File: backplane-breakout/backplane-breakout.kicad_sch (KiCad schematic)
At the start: 12 parts, among them J101 Backplane

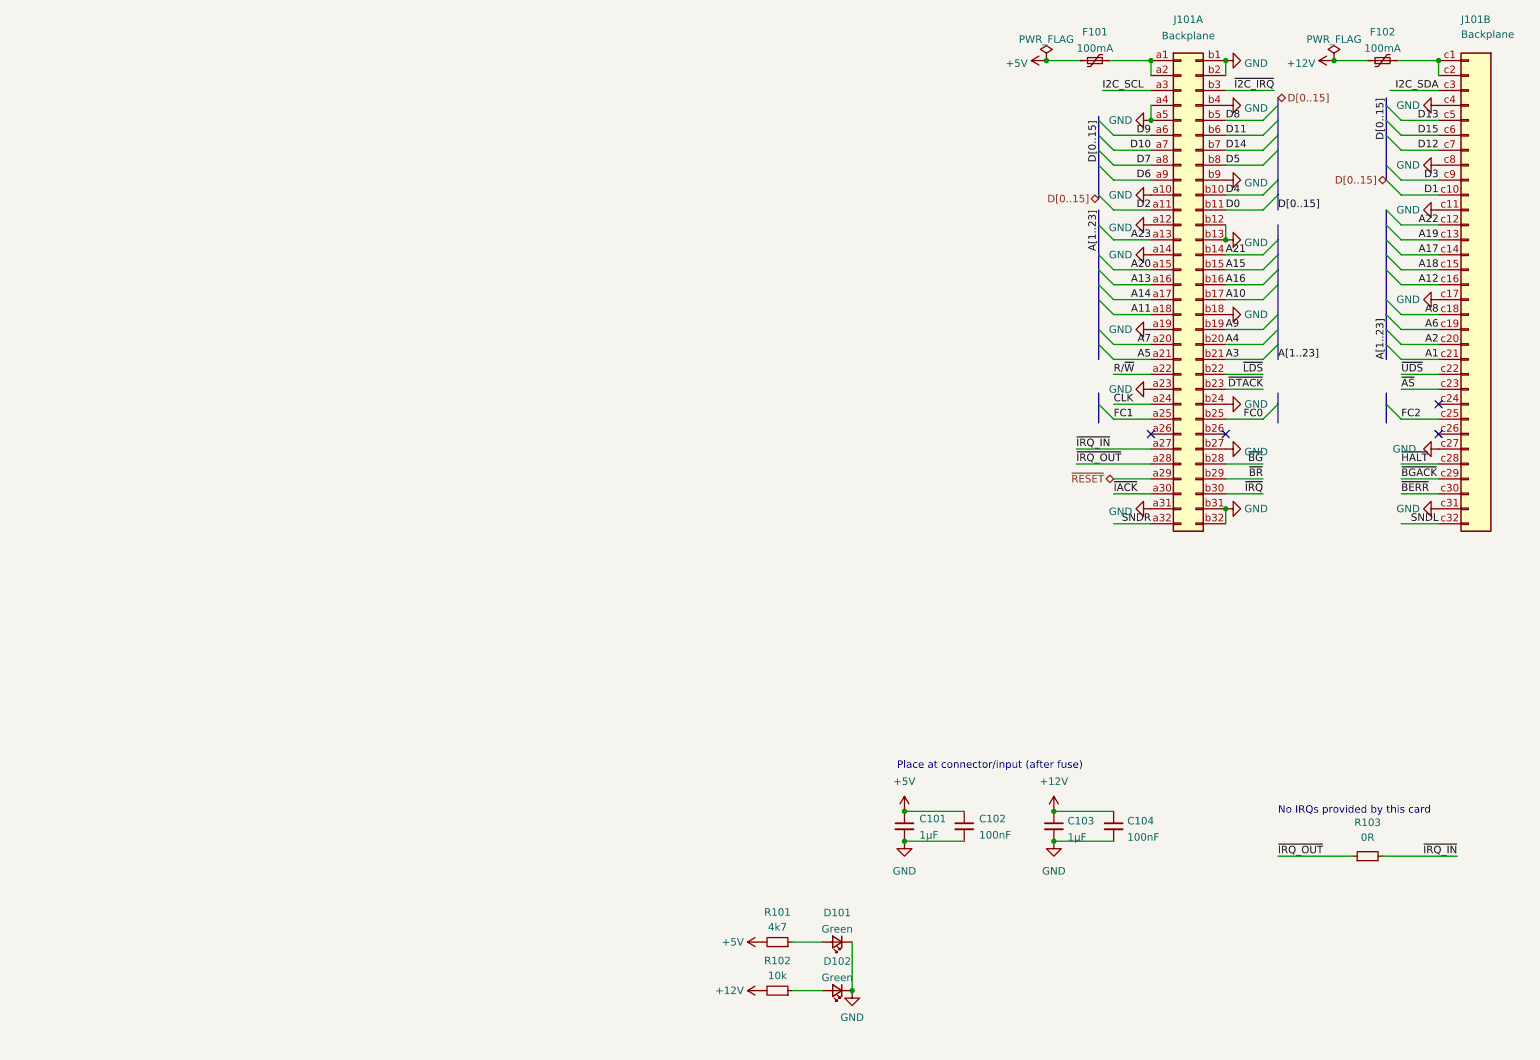
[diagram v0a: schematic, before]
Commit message: Finished backplane breakout
- All of the backplane signals (for an expansion card) are brought out
  to 2x10 headers, which can connect to the logic analyzer through
  isolation adapters or direct probing in a more compact pinout

- Added a footprint for a shrouded 2x10 header
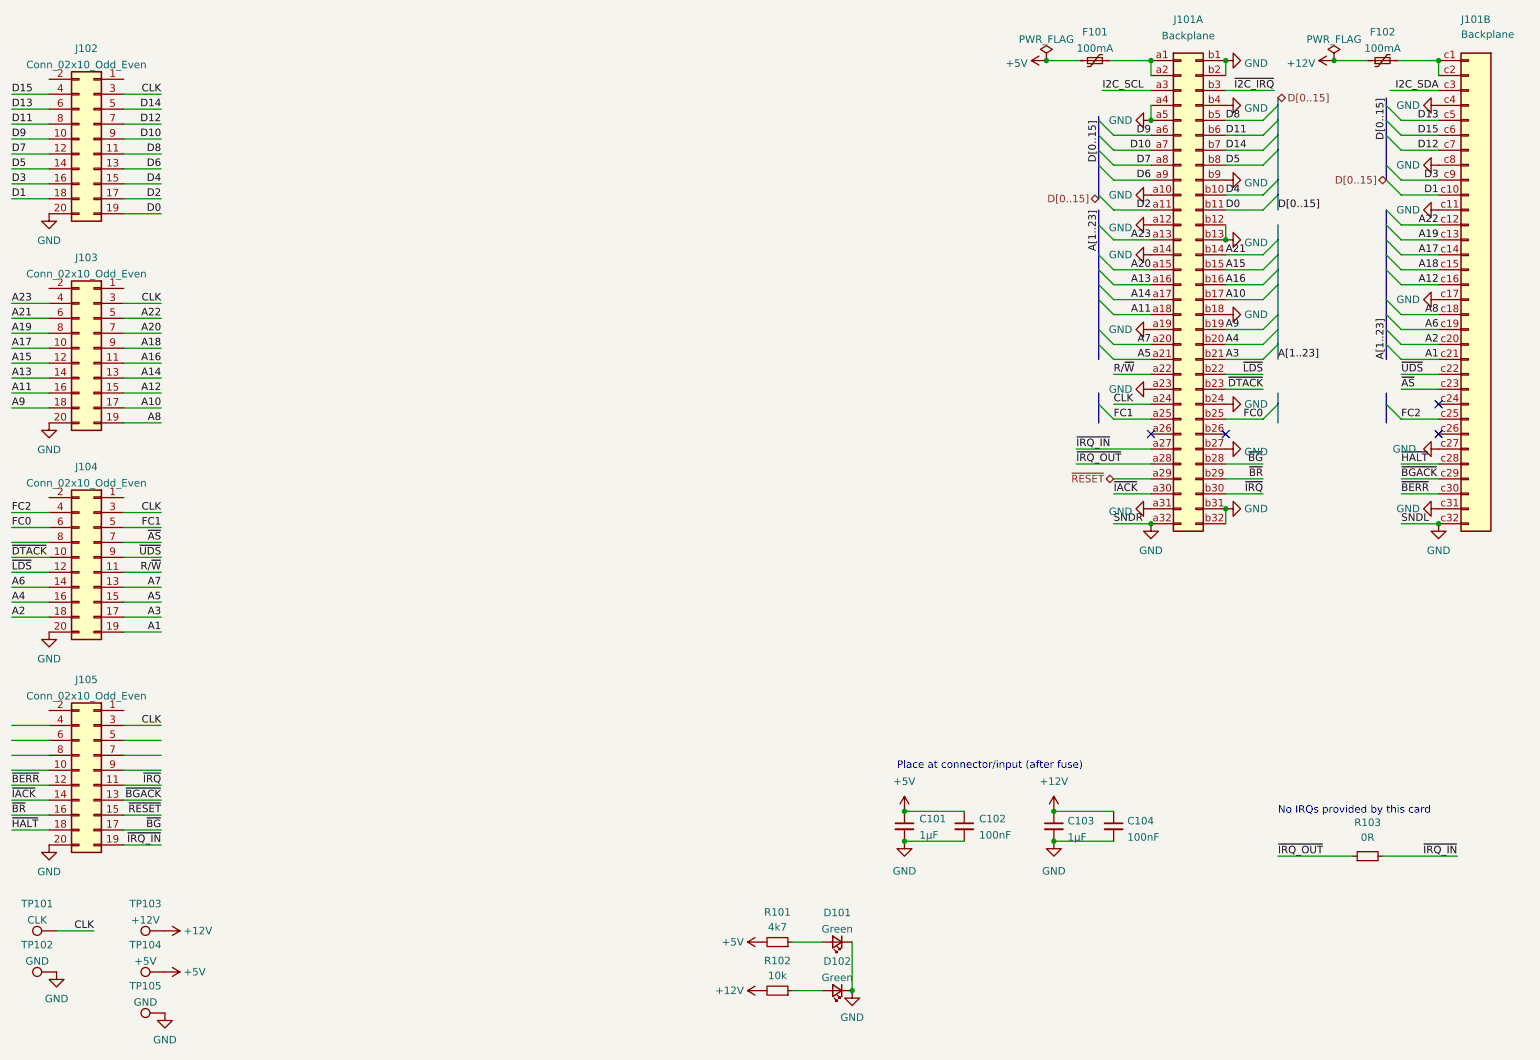
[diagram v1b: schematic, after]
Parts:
- added J102, J103, J104, J105: Conn_02x10_Odd_Even, 68komputer-common:Shrouded_PinHeader_2x10_P2.54mm_Vertical, symbol Connector_Generic:Conn_02x10_Odd_Even
- added TP101: CLK, TestPoint:TestPoint_Keystone_5000-5004_Miniature, symbol Connector:TestPoint
- added TP102, TP105: GND, TestPoint:TestPoint_Keystone_5000-5004_Miniature, symbol Connector:TestPoint
- added TP103: +12V, TestPoint:TestPoint_Keystone_5000-5004_Miniature, symbol Connector:TestPoint
- added TP104: +5V, TestPoint:TestPoint_Keystone_5000-5004_Miniature, symbol Connector:TestPoint
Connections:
- net SNDL is gone; now on net GND: J101.c32 (Pin_c32)
- net SNDR is gone; now on net GND: J101.a32 (Pin_a32)
- net +12V: now also TP103.1
- net +5V: now also TP104.1
- net A1: now also J104.19 (Pin_19)
- net A10: now also J103.17 (Pin_17)
- net A11: now also J103.16 (Pin_16)
- net A12: now also J103.15 (Pin_15)
- net A13: now also J103.14 (Pin_14)
- net A14: now also J103.13 (Pin_13)
- net A15: now also J103.12 (Pin_12)
- net A16: now also J103.11 (Pin_11)
- net A17: now also J103.10 (Pin_10)
- net A18: now also J103.9 (Pin_9)
- net A19: now also J103.8 (Pin_8)
- net A2: now also J104.18 (Pin_18)
- net A20: now also J103.7 (Pin_7)
- net A21: now also J103.6 (Pin_6)
- net A22: now also J103.5 (Pin_5)
- net A23: now also J103.4 (Pin_4)
- net A3: now also J104.17 (Pin_17)
- net A4: now also J104.16 (Pin_16)
- net A5: now also J104.15 (Pin_15)
- net A6: now also J104.14 (Pin_14)
- net A7: now also J104.13 (Pin_13)
- net A8: now also J103.19 (Pin_19)
- net A9: now also J103.18 (Pin_18)
- net CLK: now also J102.3 (Pin_3), J103.3 (Pin_3), J104.3 (Pin_3), J105.3 (Pin_3), TP101.1
- net D0: now also J102.19 (Pin_19)
- net D1: now also J102.18 (Pin_18)
- net D10: now also J102.9 (Pin_9)
- net D11: now also J102.8 (Pin_8)
- net D12: now also J102.7 (Pin_7)
- net D13: now also J102.6 (Pin_6)
- net D14: now also J102.5 (Pin_5)
- net D15: now also J102.4 (Pin_4)
- net D2: now also J102.17 (Pin_17)
- net D3: now also J102.16 (Pin_16)
- net D4: now also J102.15 (Pin_15)
- net D5: now also J102.14 (Pin_14)
- net D6: now also J102.13 (Pin_13)
- net D7: now also J102.12 (Pin_12)
- net D8: now also J102.11 (Pin_11)
- net D9: now also J102.10 (Pin_10)
- net FC0: now also J104.6 (Pin_6)
- net FC1: now also J104.5 (Pin_5)
- net FC2: now also J104.4 (Pin_4)
- net GND: now also J102.20 (Pin_20), J103.20 (Pin_20), J104.20 (Pin_20), J105.20 (Pin_20), TP102.1, TP105.1
- net R/~{W}: now also J104.11 (Pin_11)
- net ~{AS}: now also J104.7 (Pin_7)
- net ~{BERR}: now also J105.12 (Pin_12)
- net ~{BGACK}: now also J105.13 (Pin_13)
- net ~{BG}: now also J105.17 (Pin_17)
- net ~{BR}: now also J105.16 (Pin_16)
- net ~{DTACK}: now also J104.10 (Pin_10)
- net ~{HALT}: now also J105.18 (Pin_18)
- net ~{IACK}: now also J105.14 (Pin_14)
- net ~{IRQ_IN}: now also J105.19 (Pin_19)
- net ~{IRQ}: now also J105.11 (Pin_11)
- net ~{LDS}: now also J104.12 (Pin_12)
- net ~{RESET}: now also J105.15 (Pin_15)
- net ~{UDS}: now also J104.9 (Pin_9)
